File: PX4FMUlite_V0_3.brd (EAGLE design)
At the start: 48.6 x 34.9 mm, 156 parts, among them J2 DF13-4P-1.25V, J201 DF13C-6P-1.25V, J202 DF13C-6P-1.25V, J203 DF13C-6P-1.25V, J3 DF13C-4P-1.25V, J302 DF13C-4P-1.25V, J401 DF13C-4P-1.25V, J403 DF13C-7P-1.25V, J405 DF13C-4P-1.25V, J801 JST-ZH-3, J802 DF13C-3P-1.25V, M3_MOUNT1101 MOUNT-HOLE3.1MM, M3_MOUNT1102 MOUNT-HOLE3.1MM, M3_MOUNT1103 MOUNT-HOLE3.1MM, M3_MOUNT1104 MOUNT-HOLE3.1MM, U101 STM32F4X7VX, U2 MAX3051, U401 MAX3051, U903 74LVC2G240, X101 3.2x2.5 mm / 24 MHz / 15 ppm

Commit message: Hmmm
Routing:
- net N$15: track 15.9 -> 0.00 mm
- net N$16: track 14.0 -> 0.00 mm
- net N$36: track 12.2 -> 0.00 mm
- net N$68: track 10.2 -> 0.00 mm
- net N$77: track 8.39 -> 0.00 mm
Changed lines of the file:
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@@
 <contactref element="L1" pad="P$12"/>
 <contactref element="J1" pad="S5"/>
-<wire x1="19.62" y1="29.0108" x2="18.7492" y2="29.0108" width="0.2" layer="16"/>
-<wire x1="18.7492" y1="29.0108" x2="18.1864" y2="28.448" width="0.2" layer="16"/>
-<wire x1="18.1864" y1="28.448" x2="18.1864" y2="26.7208" width="0.2" layer="16"/>
-<wire x1="18.1864" y1="26.7208" x2="17.78" y2="26.3144" width="0.2" layer="16"/>
-<wire x1="17.78" y1="26.3144" x2="17.78" y2="24.2824" width="0.2" layer="16"/>
-<wire x1="17.78" y1="24.2824" x2="17.3736" y2="23.876" width="0.2" layer="16"/>
-<wire x1="17.3736" y1="23.876" x2="17.3736" y2="22.1488" width="0.2" layer="16"/>
-<wire x1="17.3736" y1="22.1488" x2="16.002" y2="20.7772" width="0.2" layer="16"/>
+<wire x1="16.002" y1="20.7772" x2="19.62" y2="29.0108" width="0" layer="19" extent="16-16"/>
 </signal>
 <signal name="N$77">
 <contactref element="L1" pad="P$13"/>
 <contactref element="J1" pad="S4"/>
-<wire x1="19.62" y1="29.5108" x2="18.4364" y2="29.5108" width="0.2" layer="16"/>
-<wire x1="18.4364" y1="29.5108" x2="17.78" y2="28.8544" width="0.2" layer="16"/>
-<wire x1="17.78" y1="28.8544" x2="17.78" y2="26.924" width="0.2" layer="16"/>
-<wire x1="17.78" y1="26.924" x2="17.3736" y2="26.5176" width="0.2" layer="16"/>
-<wire x1="17.3736" y1="26.5176" x2="17.3736" y2="24.6888" width="0.2" layer="16"/>
-<wire x1="17.3736" y1="24.6888" x2="16.002" y2="23.3172" width="0.2" layer="16"/>
+<wire x1="16.002" y1="23.3172" x2="19.62" y2="29.5108" width="0" layer="19" extent="16-16"/>
 </signal>
 <signal name="N$78">
@@
 <contactref element="L1" pad="P$9"/>
 <contactref element="J1" pad="S8"/>
-<wire x1="19.62" y1="27.5108" x2="19.586" y2="27.5108" width="0.2" layer="16"/>
-<wire x1="19.586" y1="27.5108" x2="19.4056" y2="27.3304" width="0.2" layer="16"/>
-<wire x1="19.4056" y1="27.3304" x2="19.4056" y2="26.1112" width="0.2" layer="16"/>
-<wire x1="19.4056" y1="26.1112" x2="18.9992" y2="25.7048" width="0.2" layer="16"/>
-<wire x1="18.9992" y1="25.7048" x2="18.9992" y2="23.6728" width="0.2" layer="16"/>
-<wire x1="18.9992" y1="23.6728" x2="18.5928" y2="23.2664" width="0.2" layer="16"/>
-<wire x1="18.5928" y1="23.2664" x2="18.5928" y2="21.4376" width="0.2" layer="16"/>
-<wire x1="18.5928" y1="21.4376" x2="18.1864" y2="21.0312" width="0.2" layer="16"/>
-<wire x1="18.1864" y1="21.0312" x2="18.1864" y2="18.796" width="0.2" layer="16"/>
-<wire x1="18.1864" y1="18.796" x2="17.8816" y2="18.4912" width="0.2" layer="16"/>
-<wire x1="17.8816" y1="18.4912" x2="17.8816" y2="16.8656" width="0.2" layer="16"/>
-<wire x1="17.8816" y1="16.8656" x2="17.4752" y2="16.4592" width="0.2" layer="16"/>
-<wire x1="17.4752" y1="16.4592" x2="17.4752" y2="14.6304" width="0.2" layer="16"/>
-<wire x1="17.4752" y1="14.6304" x2="16.002" y2="13.1572" width="0.2" layer="16"/>
+<wire x1="16.002" y1="13.1572" x2="19.62" y2="27.5108" width="0" layer="19" extent="16-16"/>
 </signal>
 <signal name="N$16">
 <contactref element="L1" pad="P$10"/>
 <contactref element="J1" pad="S7"/>
-<wire x1="19.62" y1="28.0108" x2="19.2732" y2="28.0108" width="0.2" layer="16"/>
-<wire x1="19.2732" y1="28.0108" x2="18.9992" y2="27.7368" width="0.2" layer="16"/>
-<wire x1="18.9992" y1="27.7368" x2="18.9992" y2="26.3144" width="0.2" layer="16"/>
-<wire x1="18.9992" y1="26.3144" x2="18.5928" y2="25.908" width="0.2" layer="16"/>
-<wire x1="18.5928" y1="25.908" x2="18.5928" y2="23.876" width="0.2" layer="16"/>
-<wire x1="18.5928" y1="23.876" x2="18.1864" y2="23.4696" width="0.2" layer="16"/>
-<wire x1="18.1864" y1="23.4696" x2="18.1864" y2="21.6408" width="0.2" layer="16"/>
-<wire x1="18.1864" y1="21.6408" x2="17.78" y2="21.2344" width="0.2" layer="16"/>
-<wire x1="17.78" y1="21.2344" x2="17.78" y2="19.1008" width="0.2" layer="16"/>
-<wire x1="17.78" y1="19.1008" x2="17.4752" y2="18.796" width="0.2" layer="16"/>
-<wire x1="17.4752" y1="18.796" x2="17.4752" y2="17.1704" width="0.2" layer="16"/>
-<wire x1="17.4752" y1="17.1704" x2="16.002" y2="15.6972" width="0.2" layer="16"/>
+<wire x1="16.002" y1="15.6972" x2="19.62" y2="28.0108" width="0" layer="19" extent="16-16"/>
 </signal>
 <signal name="N$32">
@@
 <contactref element="L1" pad="P$11"/>
 <contactref element="J1" pad="S6"/>
-<wire x1="19.62" y1="28.5108" x2="18.9604" y2="28.5108" width="0.2" layer="16"/>
-<wire x1="18.9604" y1="28.5108" x2="18.5928" y2="28.1432" width="0.2" layer="16"/>
-<wire x1="18.5928" y1="28.1432" x2="18.5928" y2="26.5176" width="0.2" layer="16"/>
-<wire x1="18.5928" y1="26.5176" x2="18.1864" y2="26.1112" width="0.2" layer="16"/>
-<wire x1="18.1864" y1="26.1112" x2="18.1864" y2="24.0792" width="0.2" layer="16"/>
-<wire x1="18.1864" y1="24.0792" x2="17.78" y2="23.6728" width="0.2" layer="16"/>
-<wire x1="17.78" y1="23.6728" x2="17.78" y2="21.844" width="0.2" layer="16"/>
-<wire x1="17.78" y1="21.844" x2="17.3736" y2="21.4376" width="0.2" layer="16"/>
-<wire x1="17.3736" y1="21.4376" x2="17.3736" y2="19.6088" width="0.2" layer="16"/>
-<wire x1="17.3736" y1="19.6088" x2="16.002" y2="18.2372" width="0.2" layer="16"/>
+<wire x1="16.002" y1="18.2372" x2="19.62" y2="28.5108" width="0" layer="19" extent="16-16"/>
 </signal>
 <signal name="N$18">

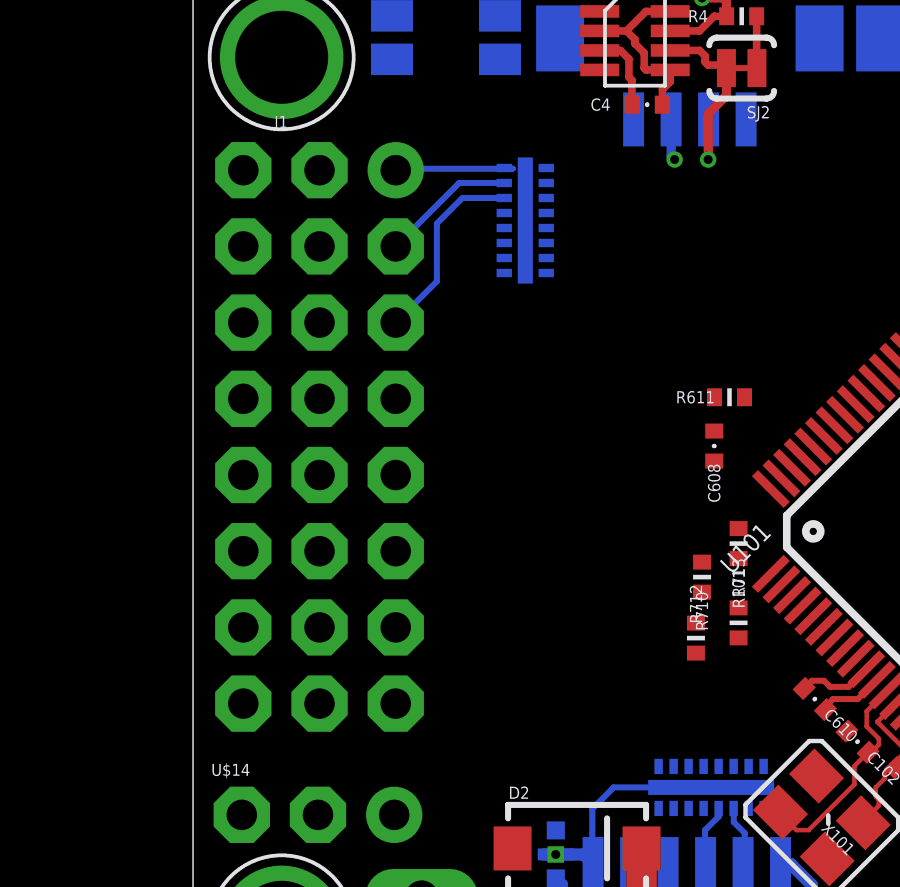
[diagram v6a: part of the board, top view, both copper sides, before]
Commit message: Rewired servo ESD a little
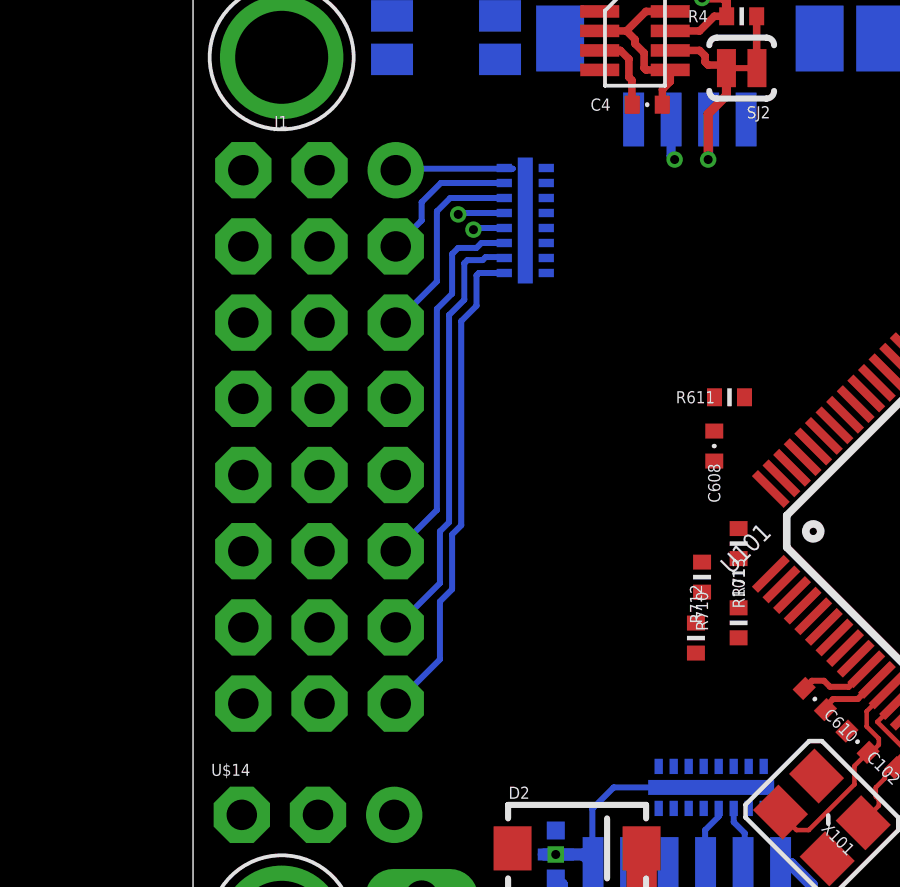
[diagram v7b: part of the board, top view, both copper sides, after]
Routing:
- net N$15: track 0.00 -> 16.3 mm
- net N$16: track 0.00 -> 14.5 mm
- net N$36: track 0.00 -> 12.6 mm
- net N$68: track 0.00 -> 10.3 mm, vias 0 -> 1
- net N$77: track 0.00 -> 8.86 mm, vias 0 -> 1
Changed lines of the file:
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@@
 <layer number="12" name="Route12" color="1" fill="5" visible="no" active="no"/>
 <layer number="13" name="Route13" color="4" fill="5" visible="no" active="no"/>
-<layer number="14" name="Vertical" color="14" fill="15" visible="no" active="yes"/>
+<layer number="14" name="Vertical" color="14" fill="15" visible="yes" active="yes"/>
 <layer number="15" name="Power" color="11" fill="15" visible="no" active="yes"/>
 <layer number="16" name="Bottom" color="1" fill="1" visible="yes" active="yes"/>
@@
 <contactref element="L1" pad="P$12"/>
 <contactref element="J1" pad="S5"/>
-<wire x1="16.002" y1="20.7772" x2="19.62" y2="29.0108" width="0" layer="19" extent="16-16"/>
+<wire x1="16.002" y1="20.7772" x2="17.8816" y2="22.6568" width="0.254" layer="14"/>
+<wire x1="17.8816" y1="22.6568" x2="17.8816" y2="28.2448" width="0.254" layer="14"/>
+<wire x1="17.8816" y1="28.2448" x2="18.5928" y2="28.956" width="0.254" layer="14"/>
+<via x="18.5928" y="28.956" extent="1-16" drill="0.3"/>
+<wire x1="18.5928" y1="28.956" x2="18.6476" y2="29.0108" width="0.2" layer="16"/>
+<wire x1="18.6476" y1="29.0108" x2="19.62" y2="29.0108" width="0.2" layer="16"/>
 </signal>
 <signal name="N$77">
 <contactref element="L1" pad="P$13"/>
 <contactref element="J1" pad="S4"/>
-<wire x1="16.002" y1="23.3172" x2="19.62" y2="29.5108" width="0" layer="19" extent="16-16"/>
+<wire x1="16.002" y1="23.3172" x2="16.51" y2="23.3172" width="0.254" layer="14"/>
+<wire x1="16.51" y1="23.3172" x2="17.3736" y2="24.1808" width="0.254" layer="14"/>
+<wire x1="17.3736" y1="24.1808" x2="17.3736" y2="28.7528" width="0.254" layer="14"/>
+<wire x1="17.3736" y1="28.7528" x2="18.0848" y2="29.464" width="0.254" layer="14"/>
+<via x="18.0848" y="29.464" extent="1-16" drill="0.3"/>
+<wire x1="18.0848" y1="29.464" x2="18.1316" y2="29.5108" width="0.2" layer="16"/>
+<wire x1="18.1316" y1="29.5108" x2="19.62" y2="29.5108" width="0.2" layer="16"/>
 </signal>
 <signal name="N$78">
 <contactref element="L1" pad="P$14"/>
 <contactref element="J1" pad="S3"/>
-<wire x1="17.3736" y1="29.1592" x2="17.3736" y2="27.2288" width="0.2" layer="16"/>
+<wire x1="17.3736" y1="29.5656" x2="17.3736" y2="27.2288" width="0.2" layer="16"/>
 <wire x1="17.3736" y1="27.2288" x2="16.002" y2="25.8572" width="0.2" layer="16"/>
-<wire x1="17.3736" y1="29.1592" x2="18.2252" y2="30.0108" width="0.2" layer="16"/>
-<wire x1="18.2252" y1="30.0108" x2="19.62" y2="30.0108" width="0.2" layer="16"/>
+<wire x1="17.3736" y1="29.5656" x2="17.8188" y2="30.0108" width="0.2" layer="16"/>
+<wire x1="17.8188" y1="30.0108" x2="19.62" y2="30.0108" width="0.2" layer="16"/>
 </signal>
 <signal name="N$79">
 <contactref element="L1" pad="P$15"/>
 <contactref element="J1" pad="S2"/>
-<wire x1="16.002" y1="28.3972" x2="18.1156" y2="30.5108" width="0.2" layer="16"/>
-<wire x1="18.1156" y1="30.5108" x2="19.62" y2="30.5108" width="0.2" layer="16"/>
+<wire x1="16.002" y1="28.3972" x2="16.8656" y2="29.2608" width="0.2" layer="16"/>
+<wire x1="16.8656" y1="29.2608" x2="16.8656" y2="29.8704" width="0.2" layer="16"/>
+<wire x1="16.8656" y1="29.8704" x2="17.506" y2="30.5108" width="0.2" layer="16"/>
+<wire x1="17.506" y1="30.5108" x2="19.62" y2="30.5108" width="0.2" layer="16"/>
 </signal>
 <signal name="FMU-CH1-PROT">
@@
 <contactref element="L1" pad="P$9"/>
 <contactref element="J1" pad="S8"/>
-<wire x1="16.002" y1="13.1572" x2="19.62" y2="27.5108" width="0" layer="19" extent="16-16"/>
+<wire x1="19.62" y1="27.5108" x2="18.7732" y2="27.5108" width="0.2" layer="16"/>
+<wire x1="18.7732" y1="27.5108" x2="18.6944" y2="27.432" width="0.2" layer="16"/>
+<wire x1="18.6944" y1="27.432" x2="18.6944" y2="26.416" width="0.2" layer="16"/>
+<wire x1="18.6944" y1="26.416" x2="18.1864" y2="25.908" width="0.2" layer="16"/>
+<wire x1="18.1864" y1="25.908" x2="18.1864" y2="19.1008" width="0.2" layer="16"/>
+<wire x1="18.1864" y1="19.1008" x2="17.8816" y2="18.796" width="0.2" layer="16"/>
+<wire x1="17.8816" y1="18.796" x2="17.8816" y2="16.9672" width="0.2" layer="16"/>
+<wire x1="17.8816" y1="16.9672" x2="17.4752" y2="16.5608" width="0.2" layer="16"/>
+<wire x1="17.4752" y1="16.5608" x2="17.4752" y2="14.6304" width="0.2" layer="16"/>
+<wire x1="17.4752" y1="14.6304" x2="16.002" y2="13.1572" width="0.2" layer="16"/>
 </signal>
 <signal name="N$16">
 <contactref element="L1" pad="P$10"/>
 <contactref element="J1" pad="S7"/>
-<wire x1="16.002" y1="15.6972" x2="19.62" y2="28.0108" width="0" layer="19" extent="16-16"/>
+<wire x1="19.62" y1="28.0108" x2="19.5892" y2="28.0416" width="0.2" layer="16"/>
+<wire x1="19.5892" y1="28.0416" x2="18.9992" y2="28.0416" width="0.2" layer="16"/>
+<wire x1="18.9992" y1="28.0416" x2="18.8976" y2="27.94" width="0.2" layer="16"/>
+<wire x1="18.8976" y1="27.94" x2="18.3896" y2="27.94" width="0.2" layer="16"/>
+<wire x1="18.3896" y1="27.94" x2="18.288" y2="27.8384" width="0.2" layer="16"/>
+<wire x1="18.288" y1="27.8384" x2="18.288" y2="26.6192" width="0.2" layer="16"/>
+<wire x1="18.288" y1="26.6192" x2="17.78" y2="26.1112" width="0.2" layer="16"/>
+<wire x1="17.78" y1="26.1112" x2="17.78" y2="19.2024" width="0.2" layer="16"/>
+<wire x1="17.78" y1="19.2024" x2="17.4752" y2="18.8976" width="0.2" layer="16"/>
+<wire x1="17.4752" y1="18.8976" x2="17.4752" y2="17.1704" width="0.2" layer="16"/>
+<wire x1="17.4752" y1="17.1704" x2="16.002" y2="15.6972" width="0.2" layer="16"/>
 </signal>
 <signal name="N$32">
@@
 <contactref element="L1" pad="P$11"/>
 <contactref element="J1" pad="S6"/>
-<wire x1="16.002" y1="18.2372" x2="19.62" y2="28.5108" width="0" layer="19" extent="16-16"/>
+<wire x1="16.002" y1="18.2372" x2="17.3736" y2="19.6088" width="0.2" layer="16"/>
+<wire x1="17.3736" y1="19.6088" x2="17.3736" y2="26.3144" width="0.2" layer="16"/>
+<wire x1="17.3736" y1="26.3144" x2="17.8816" y2="26.8224" width="0.2" layer="16"/>
+<wire x1="17.8816" y1="26.8224" x2="17.8816" y2="28.1432" width="0.2" layer="16"/>
+<wire x1="17.8816" y1="28.1432" x2="18.0848" y2="28.3464" width="0.2" layer="16"/>
+<wire x1="18.0848" y1="28.3464" x2="18.6944" y2="28.3464" width="0.2" layer="16"/>
+<wire x1="18.6944" y1="28.3464" x2="18.8588" y2="28.5108" width="0.2" layer="16"/>
+<wire x1="18.8588" y1="28.5108" x2="19.62" y2="28.5108" width="0.2" layer="16"/>
 </signal>
 <signal name="N$18">

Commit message: Getting too tight
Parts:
- moved U$16 32.7 mm to (25.2, 23.3)
- moved C7 32.6 mm to (20.7, 20.8)
- moved U$15 32.6 mm to (20.8, 23.4)
- moved C1 32.5 mm to (20.2, 27.0)
- moved C12 32.5 mm to (20.2, 29.1)
- moved C10 32.4 mm to (20.0, 13.0)
- moved C8 32.4 mm to (20.0, 16.0)
- moved C9 32.4 mm to (20.0, 18.9)
- moved R712 14.9 mm to (32.8, 28.5)
- moved R710 12.4 mm to (30.1, 29.2)
- moved R101 12.1 mm to (30.8, 27.4)
- moved JP3 11.4 mm to (51.3, 31.4), turned to 270 degrees
- moved L202 9.04 mm to (34.3, 8.23)
- moved L4 7.83 mm to (53.1, 30.9), turned to 270 degrees
- moved R713 7.40 mm to (29.5, 25.6)
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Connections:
- removed net !VDD_5V_HIPOWER_OC: U101.41
- removed net N$18: L1.P$8
- removed net N$32: L1.P$7
- new net FMU-CH6: L1.P$6, U101.62
- new net FMU-CH7: L1.P$7, U101.41
- net FMU-CH8: now also L1.P$8; no longer L1.P$6
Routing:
- net 5V_S2_FILTERED: track 0.00 -> 16.2 mm
- net GND: track 42.3 -> 53.2 mm, vias 0 -> 1
- net VDD_5V: track 10.1 -> 0.00 mm
- net FMU-CH8: track 0.00 -> 3.97 mm, vias 0 -> 1
- net FMU-CH7: track 0.00 -> 3.81 mm, vias 0 -> 1
- net FMU-CH5: track 0.00 -> 3.33 mm, vias 0 -> 1
- net FMU-CH6: track 0.00 -> 3.10 mm, vias 0 -> 1
- net FMU-CH4: track 0.00 -> 2.56 mm, vias 0 -> 1
- net FMU-CH3: track 0.00 -> 1.86 mm, vias 0 -> 1
- net FMU-CH2: track 0.00 -> 1.75 mm, vias 0 -> 1
- net !VDD_5V_VALID: track 0.00 -> 1.16 mm, vias 0 -> 1
- net FMU-CH1: track 0.00 -> 1.02 mm, vias 0 -> 1
- net N$27: track 0.00 -> 1.02 mm, vias 0 -> 1
